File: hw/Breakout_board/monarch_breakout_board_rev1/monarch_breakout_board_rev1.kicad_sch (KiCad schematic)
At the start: 26 parts, among them U2 FDC2214RGHR, U3 INA226AQDGSRQ1, U4 INA226AQDGSRQ1, Y1 SiT5000AI-2E-33N0-40

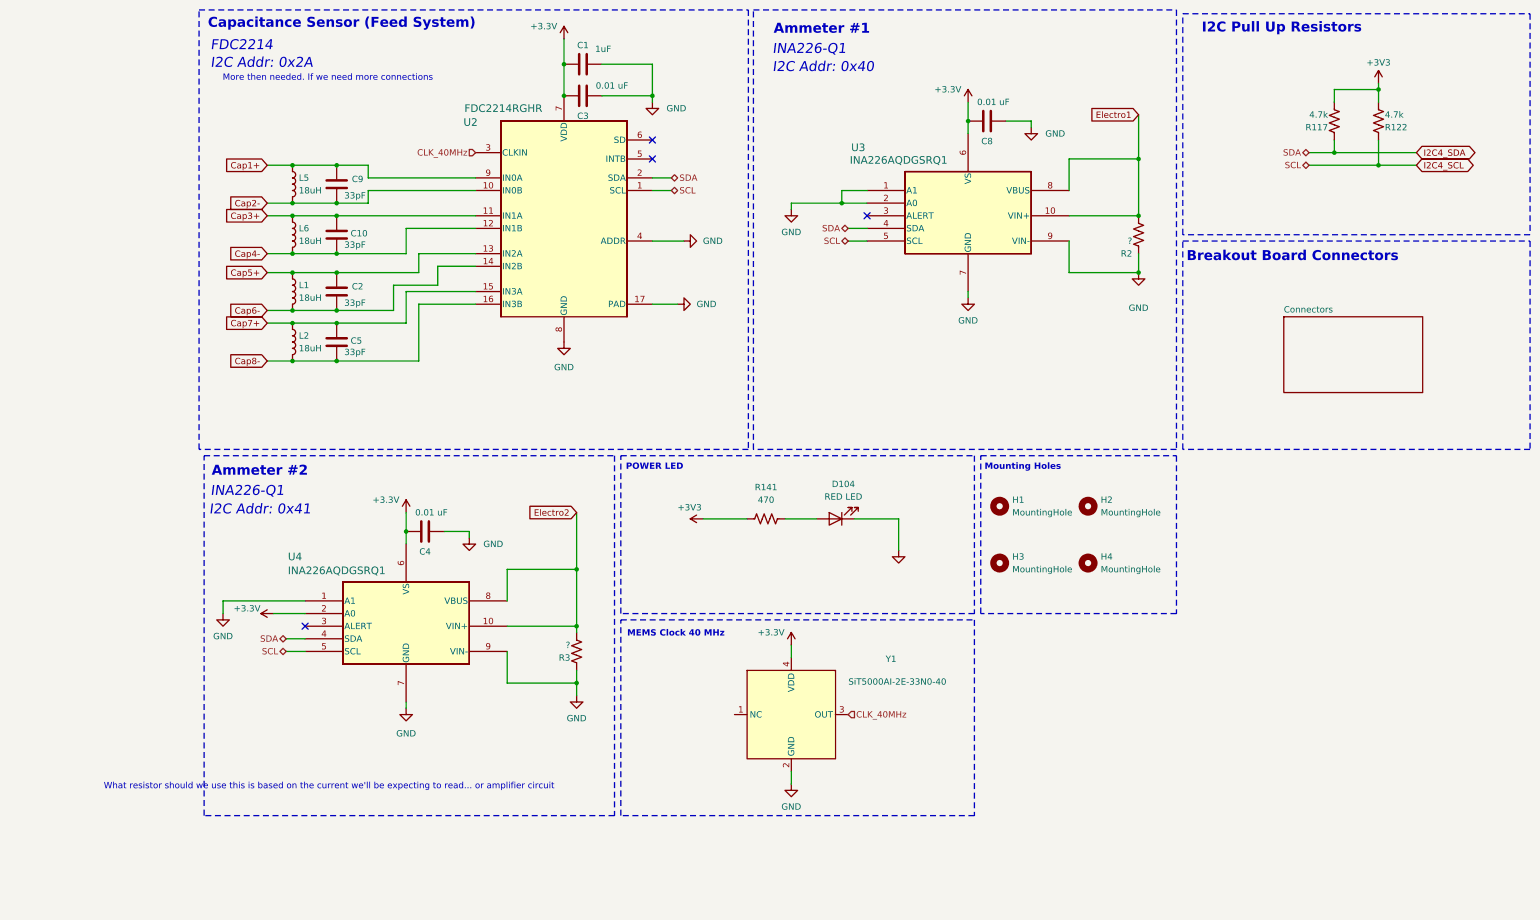
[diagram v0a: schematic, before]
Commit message: Amplifier Initial Setup / Routing Work
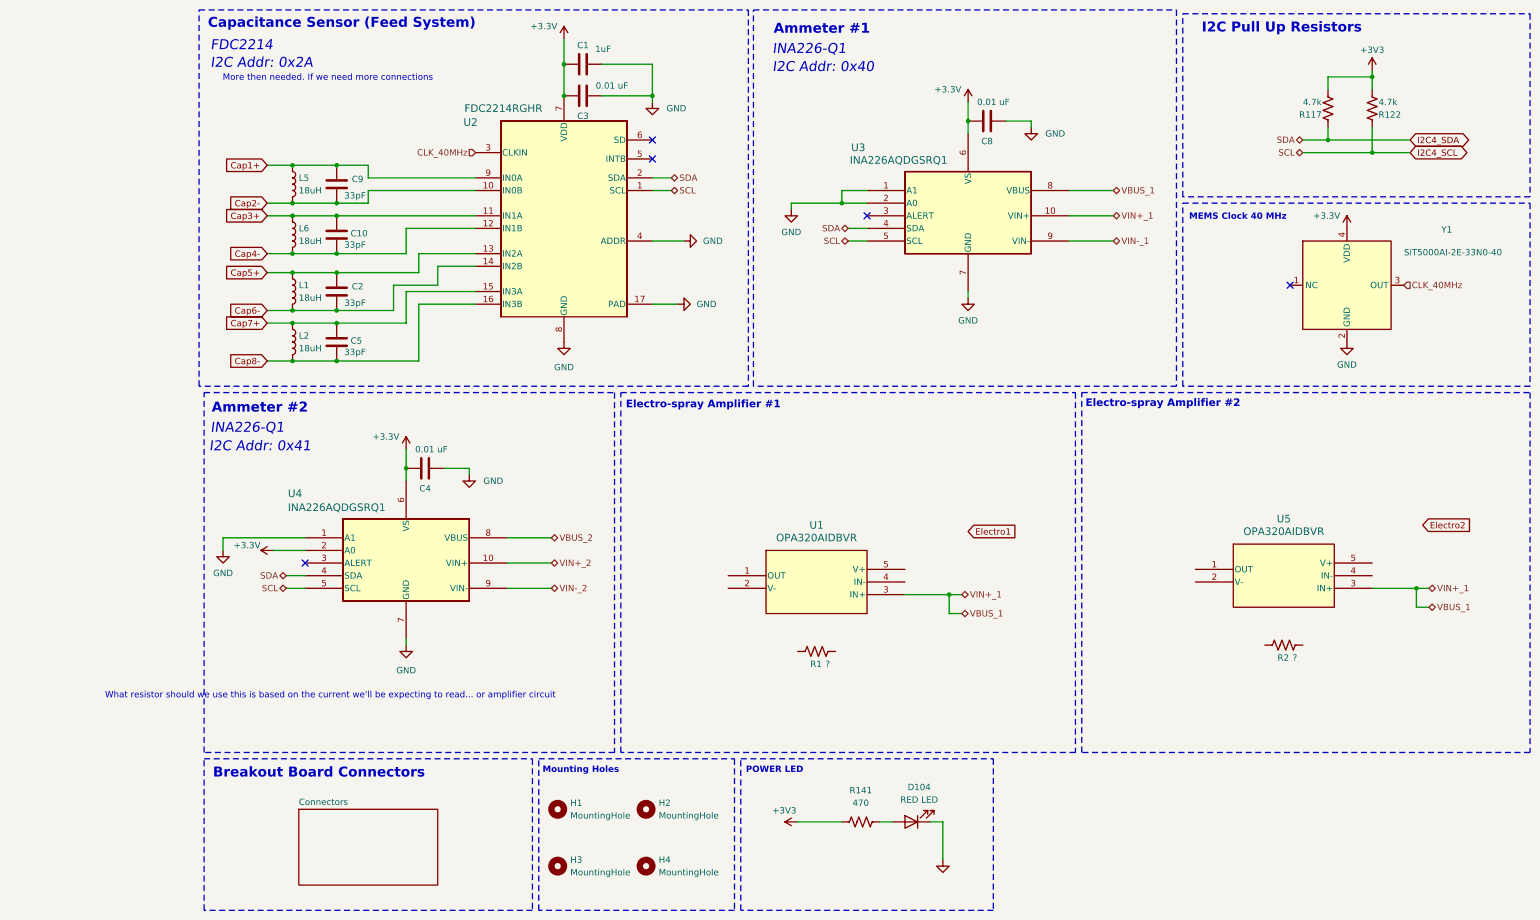
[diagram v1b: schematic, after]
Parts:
- removed R3: ?, Resistor_SMD:R_0402_1005Metric, symbol Device:R_US
- added R1: ?, Resistor_SMD:R_0402_1005Metric, symbol Device:R_US
- added U1, U5: OPA320AIDBVR, OPA320:DBV5, symbol OPA320:OPA320AIDBVR
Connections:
- net Electro1: no longer R2.1, U3.10 (VIN+), U3.8 (VBUS)
- net Electro2: no longer U4.10 (VIN+), U4.8 (VBUS)
- net GND: no longer R2.2, U3.9 (VIN-), U4.9 (VIN-)
- new net VBUS_1: U1.3 (IN+), U3.10 (VIN+), U3.8 (VBUS), U5.3 (IN+)
- new net VBUS_2: U4.8 (VBUS)
- new net VIN+_2: U4.10 (VIN+)
- new net VIN-_1: U3.9 (VIN-)
- new net VIN-_2: U4.9 (VIN-)
- no-connect marks 4 -> 5
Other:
- note added: "Electro-spray Amplifier #1"
- note added: "Electro-spray Amplifier #2"
- moved on the sheet: C4, D104, H1, H2, H3, H4, R117, R122, R141, U4, Y1

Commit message: Deletion of Components -> Ammeter Circuit Scraped + External 40 MHz Clock + Pull Up Pins on I2C
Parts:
- removed C4, C8: 0.01 uF, Capacitor_SMD:C_0603_1608Metric, symbol Device:C
- removed R1, R2: ?, Resistor_SMD:R_0402_1005Metric, symbol Device:R_US
- removed R117, R122: 4.7k, Resistor_SMD:R_0402_1005Metric, symbol Device:R_US
- removed U1, U5: OPA320AIDBVR, OPA320:DBV5, symbol OPA320:OPA320AIDBVR
- removed U3, U4: INA226AQDGSRQ1, INA226-Q1:DGS10_TEX, symbol INA226-Q1:INA226AQDGSRQ1
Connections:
- net I2C4_SCL renamed SCL
- net I2C4_SDA renamed SDA
- no-connect marks 5 -> 3
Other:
- note removed: "Ammeter #1"
- note removed: "Ammeter #2"
- note removed: "Electro-spray Amplifier #1"
- note removed: "Electro-spray Amplifier #2"
- note removed: "I2C Addr: 0x40"
- note removed: "I2C Addr: 0x41"
- note removed: "I2C Pull Up Resistors"
- note removed: "INA226-Q1"
- note removed: "What resistor should we use this is based on the current we'll be expecting to read... or amplifier circuit"
- moved on the sheet: D104, H1, H2, H3, H4, R141, Y1

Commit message: Final Breakout Board Work
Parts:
- removed Y1: SiT5000AI-2E-33N0-40, Oscillator:Oscillator_SMD_SiT_PQFN-4Pin_3.2x2.5mm, symbol SIT5000AI-2E-33N0-40.000000X:SIT5000_1
- added J2: 5037630491, Connector 4 Pin:CONN_5037630000-SD_04_MOL, symbol Connectors 4 Pin:5037630491
- added TP5, TP6, TP7, TP8: TestPoint, TestPoint:TestPoint_Keystone_5000-5004_Miniature, symbol Connector:TestPoint
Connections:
- net +3.3V is gone; now on net +3V3: C1.2, C3.2, U2.7 (VDD)
- net +3V3: now also J2.4, TP8.1
- net GND: now also J2.3, TP6.1
- net CLK_40MHz: no longer names the net of U2.3 (CLKIN)
- net SCL renamed I2C4_SCL
- net I2C4_SCL: now also J2.2, TP5.1
- net SDA renamed I2C4_SDA
- net I2C4_SDA: now also J2.1, TP7.1
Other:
- note added: "PIB Connection"
- note removed: "MEMS Clock 40 MHz"
- note removed: "More then needed. If we need more connections"
- moved on the sheet: H1, H2, H3, H4

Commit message: FIXES after Review
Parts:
- C6: renamed from C3; value 0.01 uF -> 0.1 uF
- D1: renamed from D104; footprint LED_SMD:LED_0603_1608Metric -> LED_SMD:LED_0603_1608Metric_Pad1.05x0.95mm_HandSolder
- R1: renamed from R141; value 470 -> 100; footprint Resistor_SMD:R_0402_1005Metric -> Resistor_SMD:R_0201_0603Metric_Pad0.64x0.40mm_HandSolder
- renumbered C9 to C1, C10 to C2, C2 to C3, C5 to C4, C1 to C5, H3 to H2, H2 to H3, J2 to J1, L5 to L1, L6 to L2, L1 to L3, L2 to L4, TP5 to TP1, TP6 to TP2, TP7 to TP3, TP8 to TP4, U2 to U1
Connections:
- net Cap6- is gone; now on net Cap2-: C3.2, L3.2, U1.14 (IN2B)
- net Cap7+ is gone; now on net Cap3+: C4.1, L4.1, U1.15 (IN3A)
- net Cap1+: now also C2.1, L2.1, U1.11 (IN1A); no longer C1.1, L1.1, U1.9 (IN0A)
- net Cap2-: no longer C1.2, L1.2, U1.10 (IN0B)
- net Cap3+: no longer C2.1, L2.1, U1.11 (IN1A)
- net Cap4- renamed Cap1-
- net Cap5+ renamed Cap2+
- net Cap8- renamed Cap3-
- new net Cap0+: C1.1, L1.1, U1.9 (IN0A)
- new net Cap0-: C1.2, L1.2, U1.10 (IN0B)

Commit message: FIXES V2
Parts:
- R1: footprint Resistor_SMD:R_0201_0603Metric_Pad0.64x0.40mm_HandSolder -> Resistor_SMD:R_0603_1608Metric_Pad0.98x0.95mm_HandSolder
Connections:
- net +3V3: now also J1.1; no longer J1.4
- net GND: now also J1.2; no longer J1.3
- net I2C4_SCL: now also J1.3; no longer J1.2
- net I2C4_SDA: now also J1.4; no longer J1.1
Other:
- moved on the sheet: TP1, TP2, TP3, TP4
